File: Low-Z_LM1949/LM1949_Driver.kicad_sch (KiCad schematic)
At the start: 16 parts, among them J1 Supply, J2 Input, J3 INJ_Out, Q1 BC817, Q2 TIP122, U1 LM1949N_NOPB

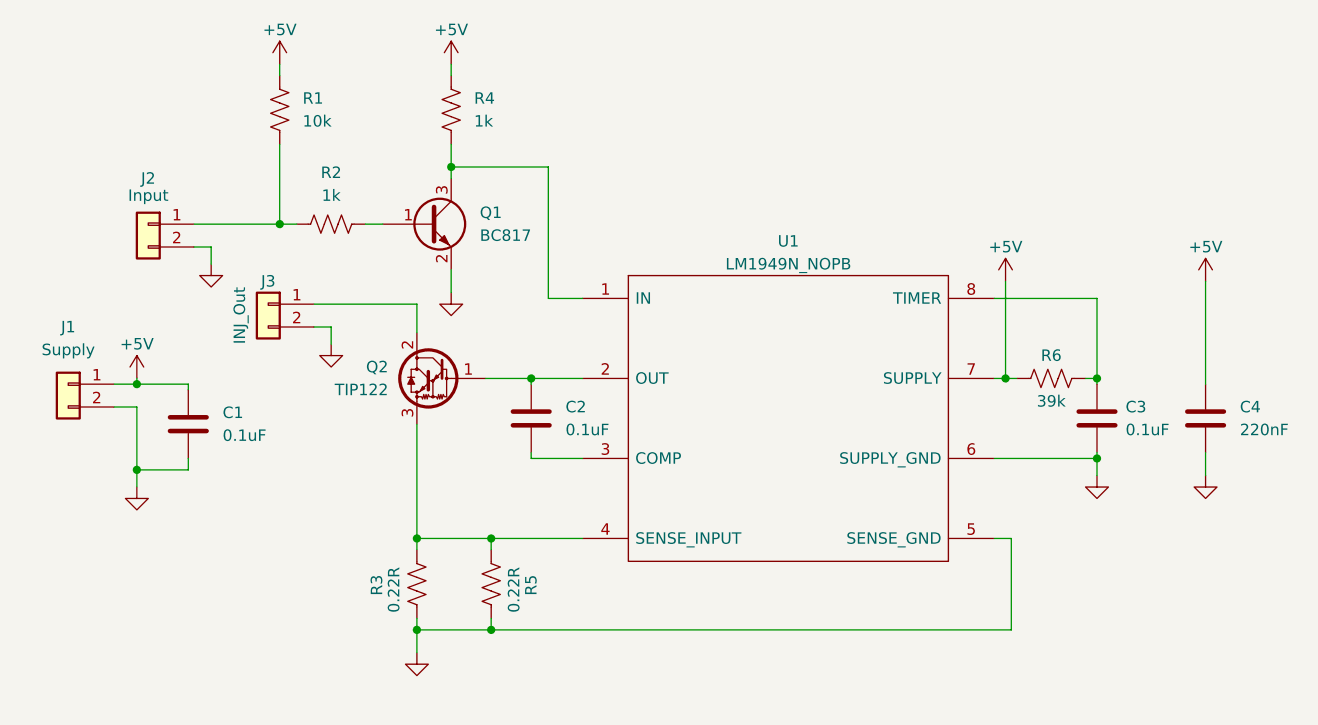
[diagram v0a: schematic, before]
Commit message: revive or recreate LM1949 driver #173
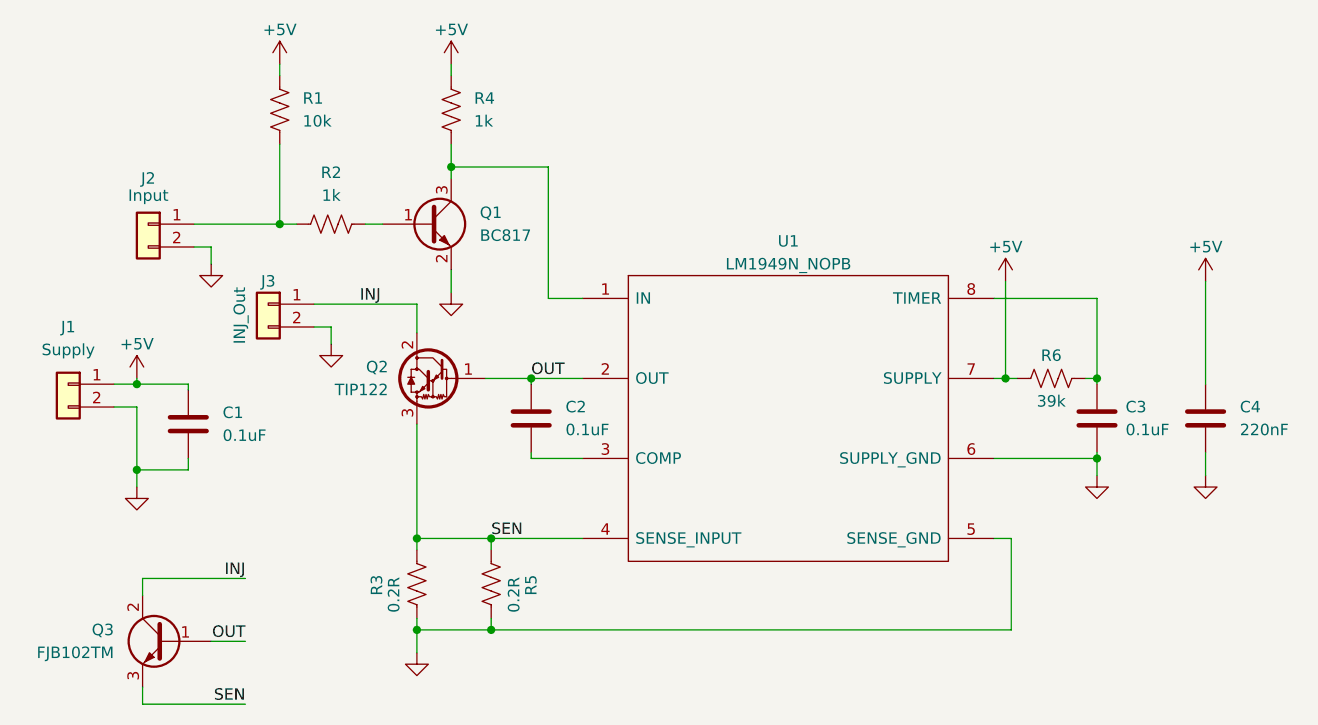
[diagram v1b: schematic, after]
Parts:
- added Q3: FJB102TM, Package_TO_SOT_SMD:TO-263-2, symbol Device:Q_NPN_BCE
- R3, R5: value 0.22R -> 0.2R; footprint Resistor_SMD:R_0805_2012Metric_Pad1.20x1.40mm_HandSolder -> Resistor_SMD:R_2512_6332Metric_Pad1.40x3.35mm_HandSolder; JLC Pt. Num C2934262 -> C176047
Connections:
- net OUT: now reaches C2.1, Q2.1 (B), U1.2 (OUT)
- net OUT: now also Q3.1 (B)
- net SEN: now reaches Q2.3 (E), R3.1, R5.1, U1.4 (SENSE_INPUT)
- net SEN: now also Q3.3 (E)
- net INJ: now reaches J3.1 (Pin_1), Q2.2 (C)
- net INJ: now also Q3.2 (C)
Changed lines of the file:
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@@
   (junction (at 117.475 106.045) (diameter 0) (color 0 0 0 0)
   )
+  (wire (pts (xy 86.995 122.555) (xy 86.995 124.46))
+    (stroke (width 0) (type default) (color 0 0 0 0))
+  )
   (wire (pts (xy 135.89 79.375) (xy 132.08 79.375))
     (stroke (width 0) (type default) (color 0 0 0 0))
@@
     (stroke (width 0) (type default) (color 0 0 0 0))
   )
+  (wire (pts (xy 86.995 124.46) (xy 98.425 124.46))
+    (stroke (width 0) (type default) (color 0 0 0 0))
+  )
   (wire (pts (xy 135.89 97.155) (xy 130.175 97.155))
     (stroke (width 0) (type default) (color 0 0 0 0))
@@
     (stroke (width 0) (type default) (color 0 0 0 0))
   )
+  (wire (pts (xy 94.615 117.475) (xy 98.425 117.475))
+    (stroke (width 0) (type default) (color 0 0 0 0))
+  )
   (wire (pts (xy 107.95 82.55) (xy 106.045 82.55))
     (stroke (width 0) (type default) (color 0 0 0 0))
@@
     (stroke (width 0) (type default) (color 0 0 0 0))
   )
+  (wire (pts (xy 86.995 112.395) (xy 86.995 110.49))
+    (stroke (width 0) (type default) (color 0 0 0 0))
+  )
   (wire (pts (xy 121.285 62.23) (xy 121.285 64.77))
     (stroke (width 0) (type default) (color 0 0 0 0))
@@
     (stroke (width 0) (type default) (color 0 0 0 0))
   )
+  (wire (pts (xy 86.995 110.49) (xy 98.425 110.49))
+    (stroke (width 0) (type default) (color 0 0 0 0))
+  )
   (wire (pts (xy 92.075 98.425) (xy 86.36 98.425))
     (stroke (width 0) (type default) (color 0 0 0 0))
@@
   (wire (pts (xy 125.73 116.205) (xy 117.475 116.205))
     (stroke (width 0) (type default) (color 0 0 0 0))
+  )
+  (label "INJ" (at 98.425 110.49 180)
+    (effects (font (size 1.27 1.27)) (justify right bottom))
+  )
+  (label "SEN" (at 98.425 124.46 180)
+    (effects (font (size 1.27 1.27)) (justify right bottom))
+  )
+  (label "SEN" (at 125.73 106.045 0)
+    (effects (font (size 1.27 1.27)) (justify left bottom))
+  )
+  (label "OUT" (at 130.175 88.265 0)
+    (effects (font (size 1.27 1.27)) (justify left bottom))
+  )
+  (label "OUT" (at 98.425 117.475 180)
+    (effects (font (size 1.27 1.27)) (justify right bottom))
+  )
+  (label "INJ" (at 111.125 80.01 0)
+    (effects (font (size 1.27 1.27)) (justify left bottom))
   )
   (symbol (lib_id "Device:R_US") (at 102.235 58.42 0) (unit 1)
@@
     (pin "1")
   )
+  (symbol (lib_id "Device:Q_NPN_BCE") (at 89.535 117.475 0) (mirror y) (unit 1)
+    (in_bom yes) (on_board yes) (fields_autoplaced)
+    (property "Reference" "Q3" (id 0) (at 83.82 116.2049 0)
+      (effects (font (size 1.27 1.27)) (justify left))
+    )
+    (property "Value" "FJB102TM" (id 1) (at 83.82 118.7449 0)
+      (effects (font (size 1.27 1.27)) (justify left))
+    )
+    (property "Footprint" "Package_TO_SOT_SMD:TO-263-2" (id 2) (at 84.455 114.935 0)
+      (effects (font (size 1.27 1.27)) hide)
+    )
+    (property "Datasheet" "~" (id 3) (at 89.535 117.475 0)
+      (effects (font (size 1.27 1.27)) hide)
+    )
+    (property "JLC Pt. Num" "NC" (id 4) (at 89.535 117.475 0)
+      (effects (font (size 1.27 1.27)) hide)
+    )
+    (pin "1")
+    (pin "2")
+    (pin "3")
+  )
   (symbol (lib_id "power:+5V") (at 102.235 53.34 0) (unit 1)
     (in_bom yes) (on_board yes)
@@
       (effects (font (size 1.27 1.27)) (justify left))
     )
-    (property "Value" "0.22R" (id 1) (at 114.935 114.3 90)
-      (effects (font (size 1.27 1.27)) (justify left))
-    )
-    (property "Footprint" "Resistor_SMD:R_0805_2012Metric_Pad1.20x1.40mm_HandSolder" (id 2) (at 118.491 111.379 90)
+    (property "Value" "0.2R" (id 1) (at 114.935 114.3 90)
+      (effects (font (size 1.27 1.27)) (justify left))
+    )
+    (property "Footprint" "Resistor_SMD:R_2512_6332Metric_Pad1.40x3.35mm_HandSolder" (id 2) (at 118.491 111.379 90)
       (effects (font (size 1.27 1.27)) hide)
     )
@@
       (effects (font (size 1.27 1.27)) hide)
     )
-    (property "JLC Pt. Num" "C2934262" (id 4) (at 117.475 111.125 0)
+    (property "JLC Pt. Num" "C176047" (id 4) (at 117.475 111.125 0)
       (effects (font (size 1.27 1.27)) hide)
     )
@@
       (effects (font (size 1.27 1.27)) (justify left))
     )
-    (property "Value" "0.22R" (id 1) (at 128.27 114.3 90)
-      (effects (font (size 1.27 1.27)) (justify left))
-    )
-    (property "Footprint" "Resistor_SMD:R_0805_2012Metric_Pad1.20x1.40mm_HandSolder" (id 2) (at 126.746 111.379 90)
+    (property "Value" "0.2R" (id 1) (at 128.27 114.3 90)
+      (effects (font (size 1.27 1.27)) (justify left))
+    )
+    (property "Footprint" "Resistor_SMD:R_2512_6332Metric_Pad1.40x3.35mm_HandSolder" (id 2) (at 126.746 111.379 90)
       (effects (font (size 1.27 1.27)) hide)
     )
@@
       (effects (font (size 1.27 1.27)) hide)
     )
-    (property "JLC Pt. Num" "C2934262" (id 4) (at 125.73 111.125 0)
+    (property "JLC Pt. Num" "C176047" (id 4) (at 125.73 111.125 0)
       (effects (font (size 1.27 1.27)) hide)
     )
@@
       (reference "Q2") (unit 1) (value "TIP122") (footprint "Package_TO_SOT_THT:TO-220-3_Vertical")
     )
+    (path "/5a1b2bee-46b4-4bfc-af14-7253a1adf718"
+      (reference "Q3") (unit 1) (value "FJB102TM") (footprint "Package_TO_SOT_SMD:TO-263-2")
+    )
     (path "/1004de67-3e6e-46aa-b068-988a98a63836"
       (reference "R1") (unit 1) (value "10k") (footprint "Resistor_SMD:R_0805_2012Metric_Pad1.20x1.40mm_HandSolder")
@@
     )
     (path "/79b5ede9-fcd6-4036-b2e1-011784c5d12b"
-      (reference "R3") (unit 1) (value "0.22R") (footprint "Resistor_SMD:R_0805_2012Metric_Pad1.20x1.40mm_HandSolder")
+      (reference "R3") (unit 1) (value "0.2R") (footprint "Resistor_SMD:R_2512_6332Metric_Pad1.40x3.35mm_HandSolder")
     )
     (path "/470b423e-e8fe-44fd-bccc-8867736a582a"
@@
     )
     (path "/98d83558-8d86-45e5-80b7-df31560a5650"
-      (reference "R5") (unit 1) (value "0.22R") (footprint "Resistor_SMD:R_0805_2012Metric_Pad1.20x1.40mm_HandSolder")
+      (reference "R5") (unit 1) (value "0.2R") (footprint "Resistor_SMD:R_2512_6332Metric_Pad1.40x3.35mm_HandSolder")
     )
     (path "/68ff83f6-cf5a-4aaa-b274-feb1c995614e"
